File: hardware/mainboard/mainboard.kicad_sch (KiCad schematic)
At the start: 1 part, among them J1 EXT

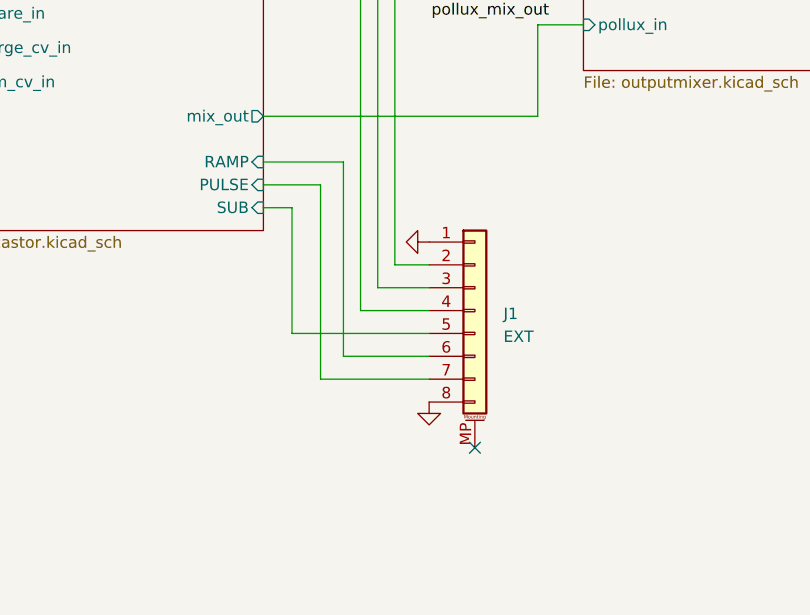
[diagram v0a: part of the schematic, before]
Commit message: Get DRC passing
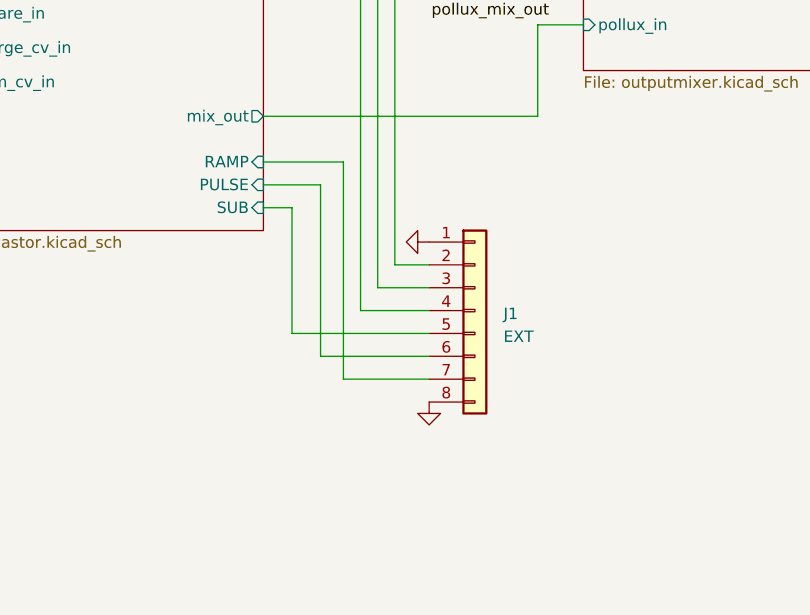
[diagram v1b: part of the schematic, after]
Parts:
- J1: footprint Connector_JST:JST_SH_BM08B-SRSS-TB_1x08-1MP_P1.00mm_Vertical -> Connector_JST:JST_GH_SM08B-GHS-TB_1x08-1MP_P1.25mm_Horizontal; symbol Connector_Generic_MountingPin:Conn_01x08_MountingPin -> Connector_Generic:Conn_01x08
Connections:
- net Pollux/PULSE: now also J1.6 (Pin_6); no longer J1.7 (Pin_7)
- net Pollux/RAMP: now also J1.7 (Pin_7); no longer J1.6 (Pin_6)
- no-connect marks 1 -> 0
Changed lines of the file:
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@@
     (comment 2 "Alethea Flowers")
   )
-  (no_connect (at 180.975 115.57))
   (wire (pts (xy 187.96 49.53) (xy 193.04 49.53))
     (stroke (width 0) (type default) (color 0 0 0 0))
@@
     (stroke (width 0) (type default) (color 0 0 0 0))
   )
+  (wire (pts (xy 163.83 105.41) (xy 163.83 86.36))
+    (stroke (width 0) (type default) (color 0 0 0 0))
+  )
   (wire (pts (xy 187.96 78.74) (xy 187.96 68.58))
     (stroke (width 0) (type default) (color 0 0 0 0))
@@
     (stroke (width 0) (type default) (color 0 0 0 0))
   )
-  (wire (pts (xy 163.83 86.36) (xy 163.83 107.95))
-    (stroke (width 0) (type default) (color 0 0 0 0))
-  )
   (wire (pts (xy 109.855 1.905) (xy 92.71 1.905))
     (stroke (width 0) (type default) (color 0 0 0 0))
   )
+  (wire (pts (xy 175.895 105.41) (xy 163.83 105.41))
+    (stroke (width 0) (type default) (color 0 0 0 0))
+  )
   (wire (pts (xy 85.09 67.31) (xy 71.12 67.31))
     (stroke (width 0) (type default) (color 0 0 0 0))
@@
     (stroke (width 0) (type default) (color 0 0 0 0))
   )
-  (wire (pts (xy 175.895 105.41) (xy 166.37 105.41))
-    (stroke (width 0) (type default) (color 0 0 0 0))
-  )
   (wire (pts (xy 71.12 44.45) (xy 104.14 44.45))
     (stroke (width 0) (type default) (color 0 0 0 0))
   )
-  (wire (pts (xy 166.37 105.41) (xy 166.37 83.82))
+  (wire (pts (xy 166.37 107.95) (xy 175.895 107.95))
+    (stroke (width 0) (type default) (color 0 0 0 0))
+  )
+  (wire (pts (xy 166.37 83.82) (xy 166.37 107.95))
     (stroke (width 0) (type default) (color 0 0 0 0))
   )
@@
   )
   (wire (pts (xy 157.48 43.18) (xy 187.96 43.18))
-    (stroke (width 0) (type default) (color 0 0 0 0))
-  )
-  (wire (pts (xy 163.83 107.95) (xy 175.895 107.95))
     (stroke (width 0) (type default) (color 0 0 0 0))
   )
@@
     (pin "1")
   )
-  (symbol (lib_id "Connector_Generic_MountingPin:Conn_01x08_MountingPin") (at 180.975 100.33 0) (unit 1)
+  (symbol (lib_id "Connector_Generic:Conn_01x08") (at 180.975 100.33 0) (unit 1)
     (in_bom yes) (on_board yes) (fields_autoplaced)
     (property "Reference" "J1" (id 0) (at 184.15 100.6855 0)
@@
       (effects (font (size 1.27 1.27)) (justify left))
     )
-    (property "Footprint" "Connector_JST:JST_SH_BM08B-SRSS-TB_1x08-1MP_P1.00mm_Vertical" (id 2) (at 180.975 100.33 0)
+    (property "Footprint" "Connector_JST:JST_GH_SM08B-GHS-TB_1x08-1MP_P1.25mm_Horizontal" (id 2) (at 180.975 100.33 0)
       (effects (font (size 1.27 1.27)) hide)
     )
@@
     (pin "7")
     (pin "8")
-    (pin "MP")
   )
   (symbol (lib_id "power:GND") (at 175.895 92.71 270) (unit 1)
@@
     )
     (path "/5bd9e93b-5109-4a41-a000-7d5082699c28"
-      (reference "J1") (unit 1) (value "EXT") (footprint "Connector_JST:JST_SH_BM08B-SRSS-TB_1x08-1MP_P1.00mm_Vertical")
+      (reference "J1") (unit 1) (value "EXT") (footprint "Connector_JST:JST_GH_SM08B-GHS-TB_1x08-1MP_P1.25mm_Horizontal")
     )
     (path "/00000000-0000-0000-0000-00005f09eaa6/00000000-0000-0000-0000-00005f0b0468"

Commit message: Swap ext connector for a vertical one
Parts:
- J1: footprint Connector_JST:JST_GH_SM08B-GHS-TB_1x08-1MP_P1.25mm_Horizontal -> Connector_JST:JST_GH_BM08B-GHS-TBT_1x08-1MP_P1.25mm_Vertical
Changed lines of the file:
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@@
       (effects (font (size 1.27 1.27)) (justify left))
     )
-    (property "Footprint" "Connector_JST:JST_GH_SM08B-GHS-TB_1x08-1MP_P1.25mm_Horizontal" (id 2) (at 180.975 100.33 0)
+    (property "Footprint" "Connector_JST:JST_GH_BM08B-GHS-TBT_1x08-1MP_P1.25mm_Vertical" (id 2) (at 180.975 100.33 0)
       (effects (font (size 1.27 1.27)) hide)
     )
@@
     )
     (path "/5bd9e93b-5109-4a41-a000-7d5082699c28"
-      (reference "J1") (unit 1) (value "EXT") (footprint "Connector_JST:JST_GH_SM08B-GHS-TB_1x08-1MP_P1.25mm_Horizontal")
+      (reference "J1") (unit 1) (value "EXT") (footprint "Connector_JST:JST_GH_BM08B-GHS-TBT_1x08-1MP_P1.25mm_Vertical")
     )
     (path "/00000000-0000-0000-0000-00005f09eaa6/00000000-0000-0000-0000-00005f0b0468"

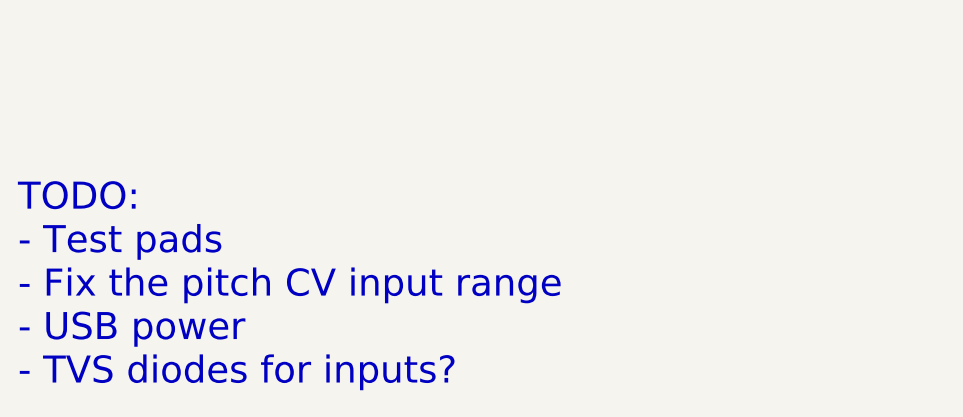
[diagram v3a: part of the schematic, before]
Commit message: Add ESD protection for inputs
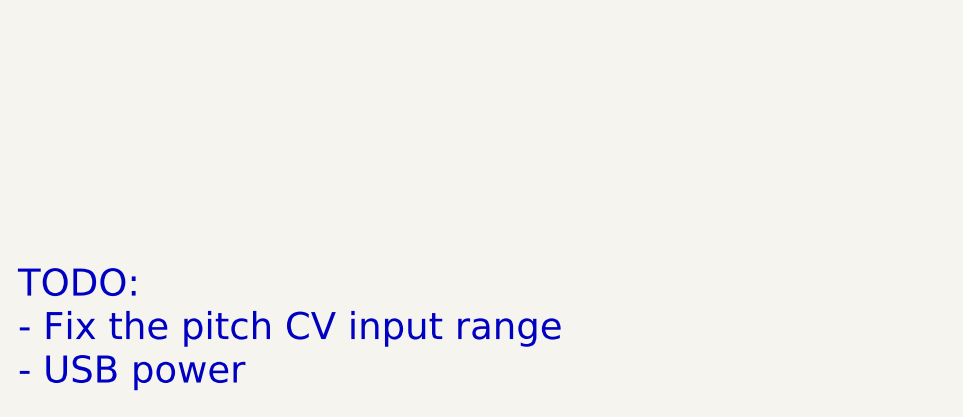
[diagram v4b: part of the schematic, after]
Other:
- note added: "TODO: - Fix the pitch CV input range - USB power"
- note removed: "TODO: - Test pads - Fix the pitch CV input range - USB power - TVS diodes for inputs?"
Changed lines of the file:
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@@
     (stroke (width 0) (type default) (color 0 0 0 0))
   )
-  (text "TODO:\n- Test pads\n- Fix the pitch CV input range\n- USB power\n- TVS diodes for inputs?"
-    (at 26.67 194.31 0)
+  (text "TODO:\n- Fix the pitch CV input range\n- USB power" (at 26.67 194.31 0)
     (effects (font (size 3 3)) (justify left bottom))
   )
@@
       (reference "#FLG0104") (unit 1) (value "PWR_FLAG") (footprint "")
     )
-    (path "/00000000-0000-0000-0000-00005f01694c/00000000-0000-0000-0000-00005f200052"
-      (reference "#PWR01") (unit 1) (value "-12V") (footprint "")
+    (path "/00000000-0000-0000-0000-00005f01694c/77f0e375-2b91-4da9-94eb-37f89e3d423c"
+      (reference "#PWR01") (unit 1) (value "GND") (footprint "")
     )
     (path "/00000000-0000-0000-0000-00005f01694c/00000000-0000-0000-0000-00005f1fa7fd"
@@
       (reference "#PWR061") (unit 1) (value "+3.3V") (footprint "")
     )
+    (path "/00000000-0000-0000-0000-00005f3674a8/a101eafe-f2f2-4f60-8ef6-c51c00711172"
+      (reference "#PWR062") (unit 1) (value "GND") (footprint "")
+    )
     (path "/00000000-0000-0000-0000-00005f09eaa6/00000000-0000-0000-0000-00005f0bf242"
       (reference "#PWR063") (unit 1) (value "GND") (footprint "")
     )
+    (path "/00000000-0000-0000-0000-00005f3674a8/a7a1661f-c036-4d29-bc74-5dc71c68b951"
+      (reference "#PWR064") (unit 1) (value "GND") (footprint "")
+    )
     (path "/00000000-0000-0000-0000-00005f09eaa6/00000000-0000-0000-0000-00005f0b7121"
       (reference "#PWR065") (unit 1) (value "GND") (footprint "")
     )
+    (path "/00000000-0000-0000-0000-00005f3674a8/f332f456-507c-4a46-852d-da87a930bc44"
+      (reference "#PWR066") (unit 1) (value "GND") (footprint "")
+    )
     (path "/00000000-0000-0000-0000-00005f09eaa6/00000000-0000-0000-0000-00005f0b3ba8"
       (reference "#PWR067") (unit 1) (value "GND") (footprint "")
     )
+    (path "/00000000-0000-0000-0000-00005f3674a8/033d3c13-5704-4fd2-9690-8b86971be163"
+      (reference "#PWR068") (unit 1) (value "GND") (footprint "")
+    )
     (path "/00000000-0000-0000-0000-00005f09eaa6/00000000-0000-0000-0000-00005f0c2670"
       (reference "#PWR069") (unit 1) (value "GND") (footprint "")
@@
     )
     (path "/00000000-0000-0000-0000-00005f01694c/00000000-0000-0000-0000-00005f07e185"
-      (reference "C2") (unit 1) (value "22uF") (footprint "Capacitor_SMD:C_0805_2012Metric_Pad1.18x1.45mm_HandSolder")
+      (reference "C2") (unit 1) (value "10u") (footprint "Capacitor_SMD:C_0805_2012Metric_Pad1.18x1.45mm_HandSolder")
     )
     (path "/00000000-0000-0000-0000-00005f01694c/00000000-0000-0000-0000-00005f07ed0e"
-      (reference "C3") (unit 1) (value "22uF") (footprint "Capacitor_SMD:C_0805_2012Metric_Pad1.18x1.45mm_HandSolder")
+      (reference "C3") (unit 1) (value "10u") (footprint "Capacitor_SMD:C_0805_2012Metric_Pad1.18x1.45mm_HandSolder")
     )
     (path "/00000000-0000-0000-0000-00005f01694c/00000000-0000-0000-0000-00005f080120"
@@
       (reference "C46") (unit 1) (value "0.1uF") (footprint "Capacitor_SMD:C_0402_1005Metric_Pad0.74x0.62mm_HandSolder")
     )
+    (path "/00000000-0000-0000-0000-00005f01694c/8ff5fb96-6b0c-4a55-9da7-fffb288dc3f7"
+      (reference "C47") (unit 1) (value "22uF") (footprint "Capacitor_SMD:C_0805_2012Metric_Pad1.18x1.45mm_HandSolder")
+    )
     (path "/00000000-0000-0000-0000-00005f01694c/00000000-0000-0000-0000-00005f1fb229"
       (reference "C48") (unit 1) (value "22uF") (footprint "Capacitor_SMD:C_0805_2012Metric_Pad1.18x1.45mm_HandSolder")
@@
       (reference "D10") (unit 1) (value "Dotstar") (footprint "winterbloom:LED_APA102_Dotstar_5050")
     )
+    (path "/00000000-0000-0000-0000-00005f3674a8/b28dcd68-b209-4884-a8ea-8de090b7a72b"
+      (reference "D11") (unit 1) (value "ESD") (footprint "Capacitor_SMD:C_0603_1608Metric_Pad1.08x0.95mm_HandSolder")
+    )
+    (path "/00000000-0000-0000-0000-00005f3674a8/e6096b4c-ad25-4cf4-a4f9-8dc2c92596f1"
+      (reference "D12") (unit 1) (value "ESD") (footprint "Capacitor_SMD:C_0603_1608Metric_Pad1.08x0.95mm_HandSolder")
+    )
+    (path "/00000000-0000-0000-0000-00005f3674a8/bfd4b1bd-0569-44bc-bed2-1855687e5012"
+      (reference "D13") (unit 1) (value "ESD") (footprint "Capacitor_SMD:C_0603_1608Metric_Pad1.08x0.95mm_HandSolder")
+    )
+    (path "/00000000-0000-0000-0000-00005f3674a8/5d9cf1c0-9c52-4334-9f79-744119a618a9"
+      (reference "D14") (unit 1) (value "ESD") (footprint "Capacitor_SMD:C_0603_1608Metric_Pad1.08x0.95mm_HandSolder")
+    )
     (path "/00000000-0000-0000-0000-00005f01694c/00000000-0000-0000-0000-00005f08907d"

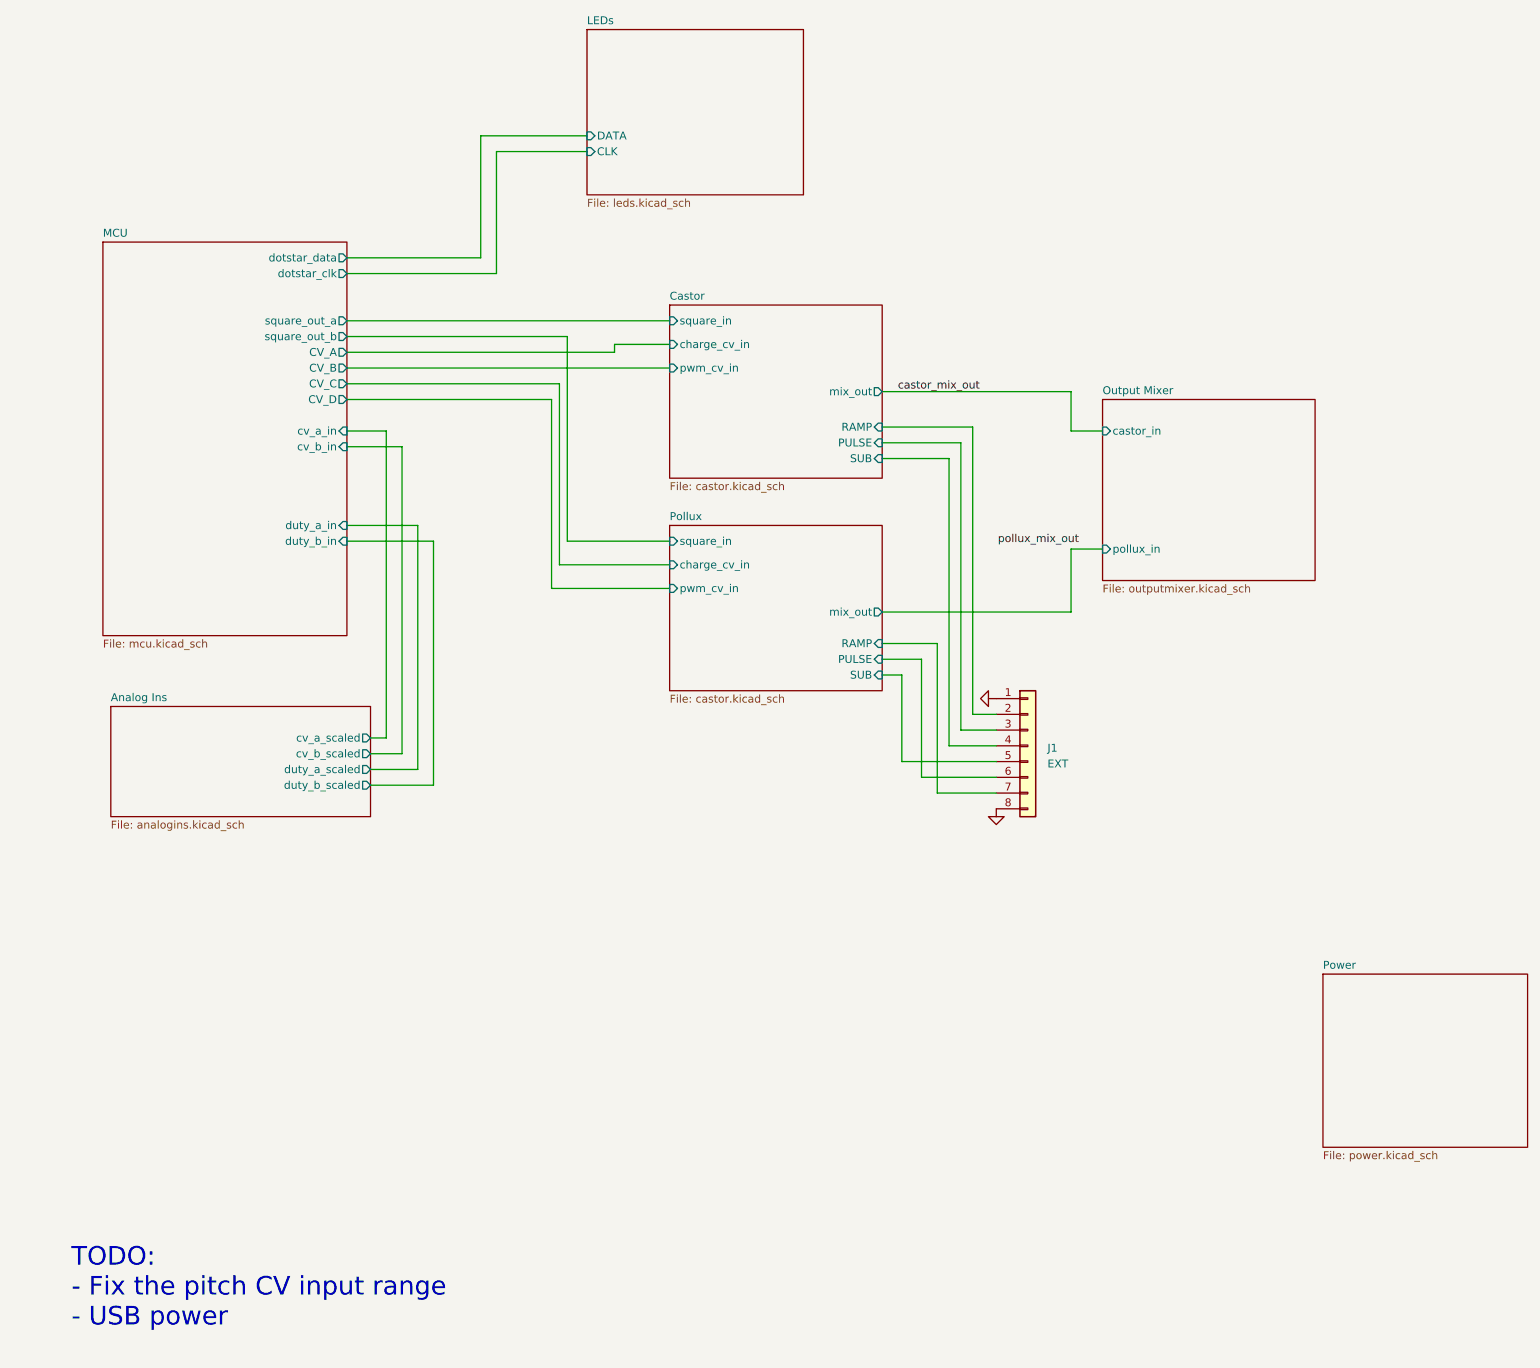
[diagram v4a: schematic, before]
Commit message: Progress on cleaning up the schematics
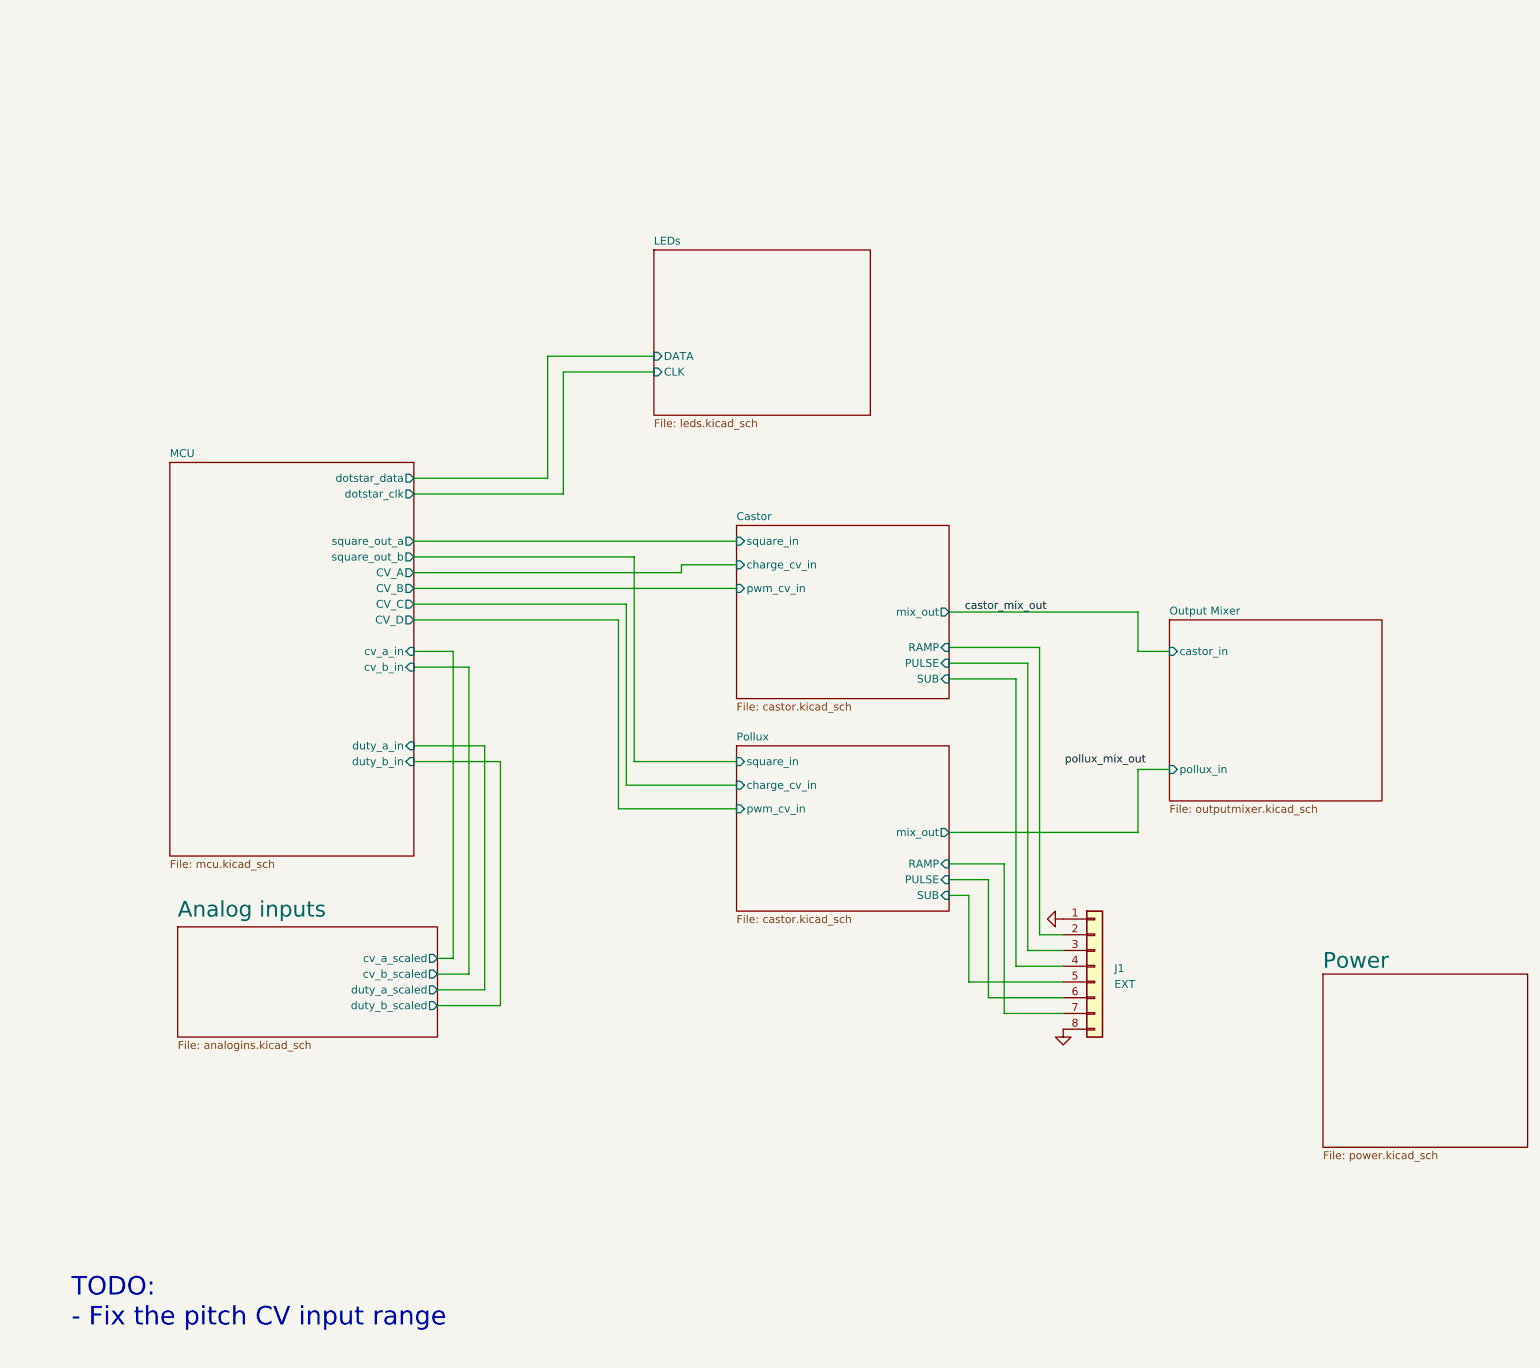
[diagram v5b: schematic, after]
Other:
- sheet Analog Ins renamed Analog inputs
- note added: "TODO: - Fix the pitch CV input range"
- note removed: "TODO: - Fix the pitch CV input range - USB power"
- moved on the sheet: J1
